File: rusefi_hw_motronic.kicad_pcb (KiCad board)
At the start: 2 copper layers, 160 x 135 mm, 48 parts, among them J1 OMEGA PCC_SMP_K, J10 Conn_01x02_Female, J2 Conn_01x02_Female, J3 Conn_01x03_Female, J4 Conn_01x03_Female, J5 Conn_01x03_Female, J6 Conn_01x03_Female, J7 Conn_01x03_Female, J8 Conn_01x04_Female, J9 Conn_01x03_Female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

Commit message: more updates
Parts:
- removed U$1: MPX4250A, Downloads:MEGASQUIRT_MPXA4250A6U
- added U6: MPXA4250A6U, rusefi_hw_motronic:MPXA4250A6U, F.Cu at (167.2, 107.4)
- moved JP3 117.3 mm to (56.5, 45.2)
- moved J4 116.6 mm to (51.9, 48.4), turned to 90 degrees
- moved JP2 109.2 mm to (56.5, 49.0)
- moved J2 16.4 mm to (32.6, 61.0)
- moved C3 6.82 mm to (160.5, 86.4)
- moved C2 6.68 mm to (165.6, 86.4), turned to 0 degrees
- moved C1 3.20 mm to (165.6, 83.7), turned to 0 degrees
- moved R1 0.32 mm to (158.6, 83.7)

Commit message: started routing
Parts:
- U1: value SFH617A-1X007T -> SFH617A-2X009T; footprint Package_DIP:DIP-4_W7.62mm -> Package_DIP:SMDIP-4_W9.53mm
- moved J6 93.0 mm to (165.1, 71.7), turned to 270 degrees
- moved J2 22.5 mm to (54.4, 66.5)
- moved R7 12.5 mm to (61.8, 120.4), turned to 0 degrees
- moved C11 12.1 mm to (56.2, 113.8)
- moved J3 11.5 mm to (64.8, 143.6), turned to 180 degrees
- moved R11 10.4 mm to (61.9, 122.9), turned to 180 degrees
- moved C10 6.91 mm to (65.3, 138.0)
- moved R8 6.85 mm to (65.3, 132.6)
- moved C12 6.73 mm to (62.0, 138.0)
- moved R12 6.65 mm to (62.0, 132.6)
- moved R3 6.19 mm to (174.8, 62.4), turned to 270 degrees
- moved JP1 6.14 mm to (58.4, 41.9), turned to 270 degrees
- moved U1 5.11 mm to (169.9, 56.6)
- moved JP3 4.32 mm to (56.4, 49.5)
- moved R4 3.81 mm to (66.1, 93.1), turned to 270 degrees
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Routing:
- net +5V: track 0.00 -> 163.4 mm, vias 0 -> 1
- net IGN_SWITCH: track 0.00 -> 143.1 mm, vias 0 -> 1
- net BARO: track 0.00 -> 77.0 mm
- net INJ_1: track 0.00 -> 74.7 mm, vias 0 -> 2
- net INJ_2: track 0.00 -> 72.7 mm
- net IGN1: track 0.00 -> 64.8 mm
- net IGN_C: track 0.00 -> 56.2 mm
- net IGN_B: track 0.00 -> 55.5 mm
- net SCK: track 0.00 -> 47.0 mm
- net IAC_CLOSE: track 0.00 -> 46.7 mm
- net ETB-: track 0.00 -> 45.4 mm
- net CAN_H: track 0.00 -> 45.0 mm
- net CAN_L: track 0.00 -> 44.0 mm
- net IAC_OPEN: track 0.00 -> 40.9 mm
- net ETB+: track 0.00 -> 39.8 mm
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- added copper zone on B.Cu, net GND
- added copper zone on F.Cu, net GND

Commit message: finished routing
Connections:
- net USB_DM renamed USB-
- net USB_DP renamed USB+
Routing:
- net SENSOR_GND: track 0.00 -> 477.0 mm, vias 0 -> 14
- net AC_ON_INPUT: track 0.00 -> 163.8 mm, vias 0 -> 2
- net CAM: track 0.00 -> 147.5 mm, vias 0 -> 6
- net +12V: track 0.00 -> 146.6 mm, vias 0 -> 4
- net TPS: track 26.6 -> 171.6 mm, vias 1 -> 3
- net +5V: track 163.4 -> 307.0 mm, vias 1 -> 3
- net OIL_PRESSURE: track 0.00 -> 108.9 mm
- net FAN_PWM: track 0.00 -> 103.7 mm
- net OIL_TEMP: track 0.00 -> 103.3 mm, vias 0 -> 2
- net USB-: track 0.00 -> 93.6 mm
- net USB+: track 0.00 -> 91.0 mm, vias 0 -> 1
- net FUEL_PUMP: track 8.58 -> 74.7 mm
- net AC_IDLE_IN: track 3.58 -> 64.8 mm, vias 0 -> 1
- net CS_KNOCK: track 3.23 -> 63.0 mm, vias 0 -> 1
- net TACH_OUT: track 0.00 -> 58.5 mm, vias 0 -> 1
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
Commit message: added rusefi logo
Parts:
- added G***: LOGO, rusefi_motronic:rusefi_logo, F.Cu at (34.0, 57.1)
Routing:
- net +5V: track 307.0 -> 317.1 mm, vias 3 -> 4

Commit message: updated etb traces
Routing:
- net ETB-: track 45.4 -> 41.7 mm
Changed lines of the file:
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@@
   )
   (setup
-    (last_trace_width 0.4064)
+    (last_trace_width 1.2192)
     (user_trace_width 0.2)
     (user_trace_width 0.254)
@@
   (segment (start 153.869201 40.077201) (end 157.988 44.196) (width 0.4064) (layer B.Cu) (net 2))
   (segment (start 141.668201 40.077201) (end 153.869201 40.077201) (width 0.4064) (layer B.Cu) (net 2))
-  (segment (start 157.988 31.496) (end 157.988 44.196) (width 0.4064) (layer B.Cu) (net 2) (status 1000000))
-  (segment (start 117.865 33.274) (end 120.913 30.226) (width 0.4064) (layer B.Cu) (net 2) (status 1000000))
-  (segment (start 120.913 30.226) (end 156.718 30.226) (width 0.4064) (layer B.Cu) (net 2) (status 1000000))
-  (segment (start 156.718 30.226) (end 157.988 31.496) (width 0.4064) (layer B.Cu) (net 2) (status 1000000))
+  (segment (start 157.988 31.496) (end 157.988 44.196) (width 0.4064) (layer B.Cu) (net 2))
+  (segment (start 117.865 33.274) (end 120.913 30.226) (width 0.4064) (layer B.Cu) (net 2))
+  (segment (start 120.913 30.226) (end 156.718 30.226) (width 0.4064) (layer B.Cu) (net 2))
+  (segment (start 156.718 30.226) (end 157.988 31.496) (width 0.4064) (layer B.Cu) (net 2))
   (segment (start 159.5755 90.678) (end 159.5755 83.693) (width 0.4064) (layer F.Cu) (net 3))
   (segment (start 52.5145 92.8385) (end 52.516 92.837) (width 0.4064) (layer F.Cu) (net 4))
@@
   (segment (start 43.235 84.132) (end 46.606 87.503) (width 0.9144) (layer F.Cu) (net 16))
   (segment (start 42.418 84.132) (end 43.235 84.132) (width 0.9144) (layer F.Cu) (net 16))
-  (segment (start 93.457 69.215) (end 90.028 72.644) (width 0.6096) (layer F.Cu) (net 17))
-  (segment (start 63.754 72.644) (end 57.5945 66.4845) (width 0.6096) (layer F.Cu) (net 17))
-  (segment (start 90.028 72.644) (end 63.754 72.644) (width 0.6096) (layer F.Cu) (net 17))
-  (segment (start 97.157 69.215) (end 94.452199 71.919801) (width 0.6096) (layer F.Cu) (net 18))
-  (segment (start 92.3975 73.9745) (end 97.157 69.215) (width 0.6096) (layer F.Cu) (net 18))
-  (segment (start 57.5945 73.9745) (end 92.3975 73.9745) (width 0.6096) (layer F.Cu) (net 18))
+  (segment (start 63.334601 72.224601) (end 57.5945 66.4845) (width 1.2192) (layer F.Cu) (net 17))
+  (segment (start 90.447399 72.224601) (end 63.334601 72.224601) (width 1.2192) (layer F.Cu) (net 17))
+  (segment (start 93.457 69.215) (end 90.447399 72.224601) (width 1.2192) (layer F.Cu) (net 17))
+  (segment (start 57.788 74.168) (end 57.5945 73.9745) (width 1.2192) (layer F.Cu) (net 18))
+  (segment (start 92.204 74.168) (end 57.788 74.168) (width 1.2192) (layer F.Cu) (net 18))
+  (segment (start 97.157 69.215) (end 92.204 74.168) (width 1.2192) (layer F.Cu) (net 18))
   (segment (start 54.664 48.494) (end 55.7 49.53) (width 0.4064) (layer F.Cu) (net 19))
   (segment (start 51.943 48.494) (end 54.664 48.494) (width 0.4064) (layer F.Cu) (net 19))

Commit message: more layout updates
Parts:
- added BT1: Battery_Cell, Battery:BatteryHolder_Keystone_1060_1x2032, F.Cu at (164.8, 131.1)
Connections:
- U3 pad J31: (no net) -> RTC_BATT+
- U3 pad J32: (no net) -> RTC_BATT-
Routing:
- net RTC_BATT+: track 0.00 -> 58.5 mm
- net RTC_BATT-: track 0.00 -> 48.8 mm
- net SENSOR_GND: track 477.0 -> 497.0 mm
- net AC_ON_INPUT: track 163.8 -> 155.6 mm
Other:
- board text added: "0.1 2020-07-14"
- board text added: "CAM"
- board text added: "CAN"
- board text added: "FAN"
- board text added: "IGN"
- board text added: "KNOCK"
- board text added: "Motronic Interface Board"
- board text added: "OIL"
- board text added: "TPS"
- board text added: "USB"

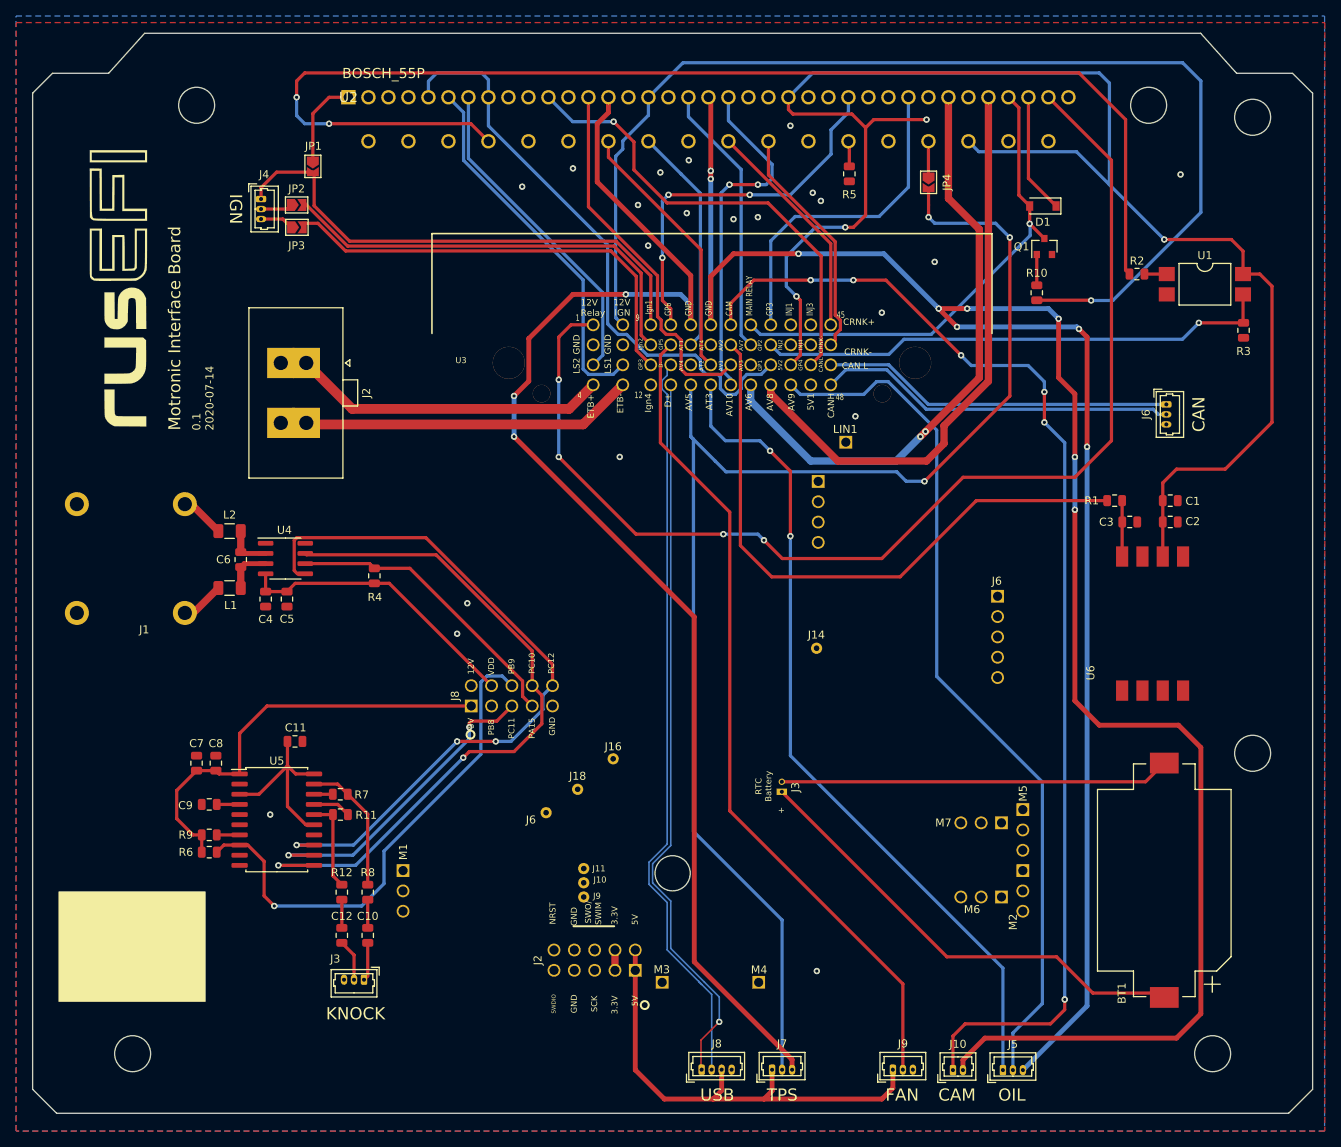
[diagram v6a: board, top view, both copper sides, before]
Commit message: improved routing
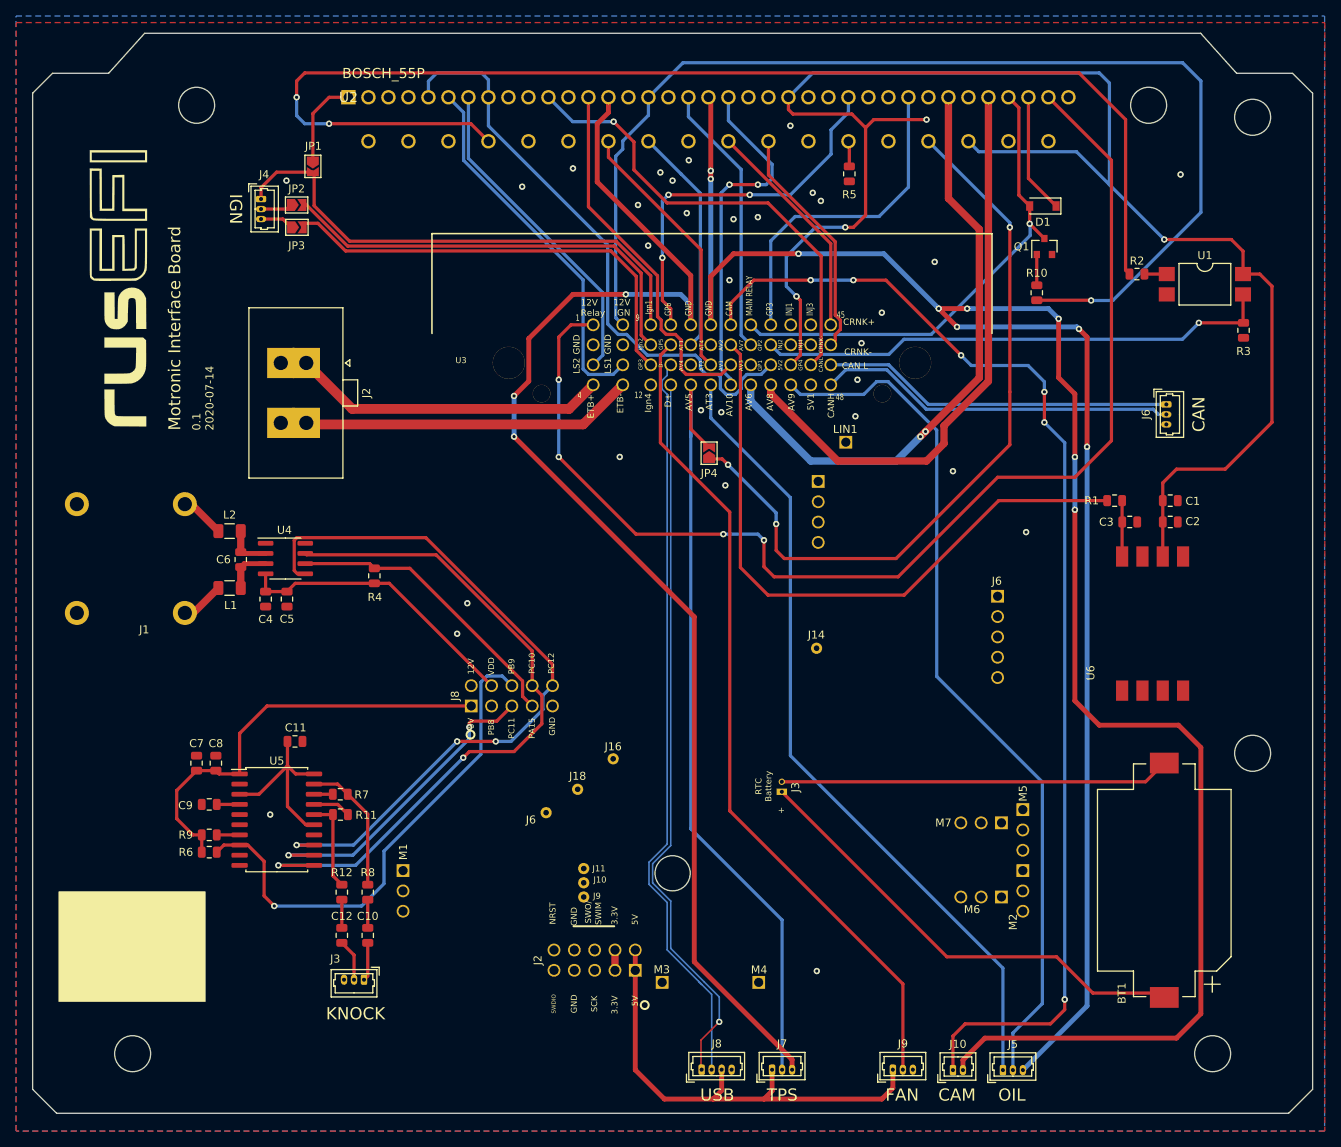
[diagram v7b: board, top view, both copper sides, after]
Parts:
- moved JP4 43.6 mm to (108.0, 77.8), turned to 90 degrees
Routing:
- net Net-(JP4-Pad1): track 4.41 -> 93.5 mm, vias 0 -> 3
- net TPS: track 171.6 -> 99.9 mm, vias 3 -> 0
- net +12V: track 146.6 -> 150.4 mm
- net BARO: track 77.0 -> 80.5 mm
- net OIL_TEMP: track 103.3 -> 100.8 mm, vias 2 -> 0
- net GND: vias 16 -> 30
- net (no net): vias 5 -> 1
